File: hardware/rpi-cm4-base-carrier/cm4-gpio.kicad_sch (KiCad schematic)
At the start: 5 parts

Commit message: Finished schematic
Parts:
- removed F?: 0ZCG0150AF2C, footprints:0ZCG0150AF2C, symbol 2020-11-06_00-20-18:0ZCG0150AF2C
- added CR1: SMBJ5.0A-TR, footprints:SMBJ5.0A-TR, symbol 2020-11-06_22-01-36:SMBJ5.0A-TR
- added D1: LED Green, LED_SMD:LED_0603_1608Metric, symbol Device:LED
- added D2: LED Red, LED_SMD:LED_0603_1608Metric, symbol Device:LED
- added J1: DNP, Connector_PinHeader_2.54mm:PinHeader_1x10_P2.54mm_Vertical, symbol Connector_Generic:Conn_01x10
- added J3: SM04B-SRSS-TB(LF)(SN), SM04B-SRSS-TB_LF__SN_:JST_SM04B-SRSS-TB(LF)(SN), symbol SM04B-SRSS-TB_LF__SN_:SM04B-SRSS-TB(LF)(SN)
- added JP1: SolderJumper_2_Open, Jumper:SolderJumper-2_P1.3mm_Open_RoundedPad1.0x1.5mm, symbol Jumper:SolderJumper_2_Open
- added R2, R6: 1k, Resistor_SMD:R_0603_1608Metric_Pad0.98x0.95mm_HandSolder, symbol Device:R
- added R3, R5: DNP, Resistor_SMD:R_0603_1608Metric_Pad0.98x0.95mm_HandSolder, symbol Device:R
- added U1: 74LVC1G07SE-7, Package_TO_SOT_SMD:SOT-353_SC-70-5, symbol CM4IO:74LVC1G07_copy
- J2: renamed from J?; footprint GCT_USB4105-GF-A -> USB4105-GF-A:GCT_USB4105-GF-A
- gave numbers to parts that had none: 2
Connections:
- net +3.3V: now also Module1.78 (GPIO_VREF(1.8v/3.3v_Input)), D1.2 (A), D2.2 (A), J1.1 (Pin_1), J3.2, R3.1, R5.1, U1.5 (VCC)
- net +5V: now also J2.A4/B9 (VBUS), J2.B4/A9 (VBUS), CR1.1
- net GND: now also CR1.2, J1.2 (Pin_2), J3.1, J3.4, JP1.2 (B), R5.2, U1.3 (GND)
- net EEPROM_nWP: now reaches Module1.20 (EEPROM_nWP)
- net EEPROM_nWP: now also JP1.1 (A)
- net nLED_Activity: now reaches Module1.21 (PI_nLED_Activity)
- net nLED_Activity: now also R2.2
- net GPIO7: now reaches Module1.37 (GPIO7)
- net GPIO7: now also J1.9 (Pin_9)
- net GPIO11: now reaches Module1.38 (GPIO11)
- net GPIO11: now also J1.7 (Pin_7)
- net GPIO8: now reaches Module1.39 (GPIO8)
- net GPIO8: now also J1.8 (Pin_8)
- net GPIO9: now reaches Module1.40 (GPIO9)
- net GPIO9: now also J1.6 (Pin_6)
- net GPIO10: now reaches Module1.44 (GPIO10)
- net GPIO10: now also J1.5 (Pin_5)
- net GPIO15: now reaches Module1.51 (GPIO15)
- net GPIO15: now also J1.4 (Pin_4)
- net GPIO14: now reaches Module1.55 (GPIO14)
- net GPIO14: now also J1.3 (Pin_3)
- net GPIO2: now reaches Module1.58 (GPIO2)
- net GPIO2: now also J3.3, R3.2
- net nRPIBOOT: now reaches Module1.93 (nRPIBOOT)
- net nRPIBOOT: now also J1.10 (Pin_10)
- net nPWR_LED: now reaches Module1.95 (nPI_LED_PWR)
- net nPWR_LED: now also U1.2
- new net: D2.1 (K), R6.1
- new net: J3.S1 (SHIELD), J3.S2 (SHIELD)
- new net: R6.2, U1.4
- new net: D1.1 (K), R2.1
- no-connect marks 6 -> 7
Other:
- note added: "Activity LED"
- note added: "I2C1_SCL"
- note added: "I2C1_SDA"
- note added: "PWR LED"
- note added: "SPI0_CE0"
- note added: "SPI0_CE1"
- note added: "SPI0_CLK"
- note added: "SPI0_MISO"
- note added: "SPI0_MOSI"
- note added: "UART0_RXD"
- note added: "UART0_TXD"
- note added: "nBOOT"
- moved on the sheet: J2, R1, R4

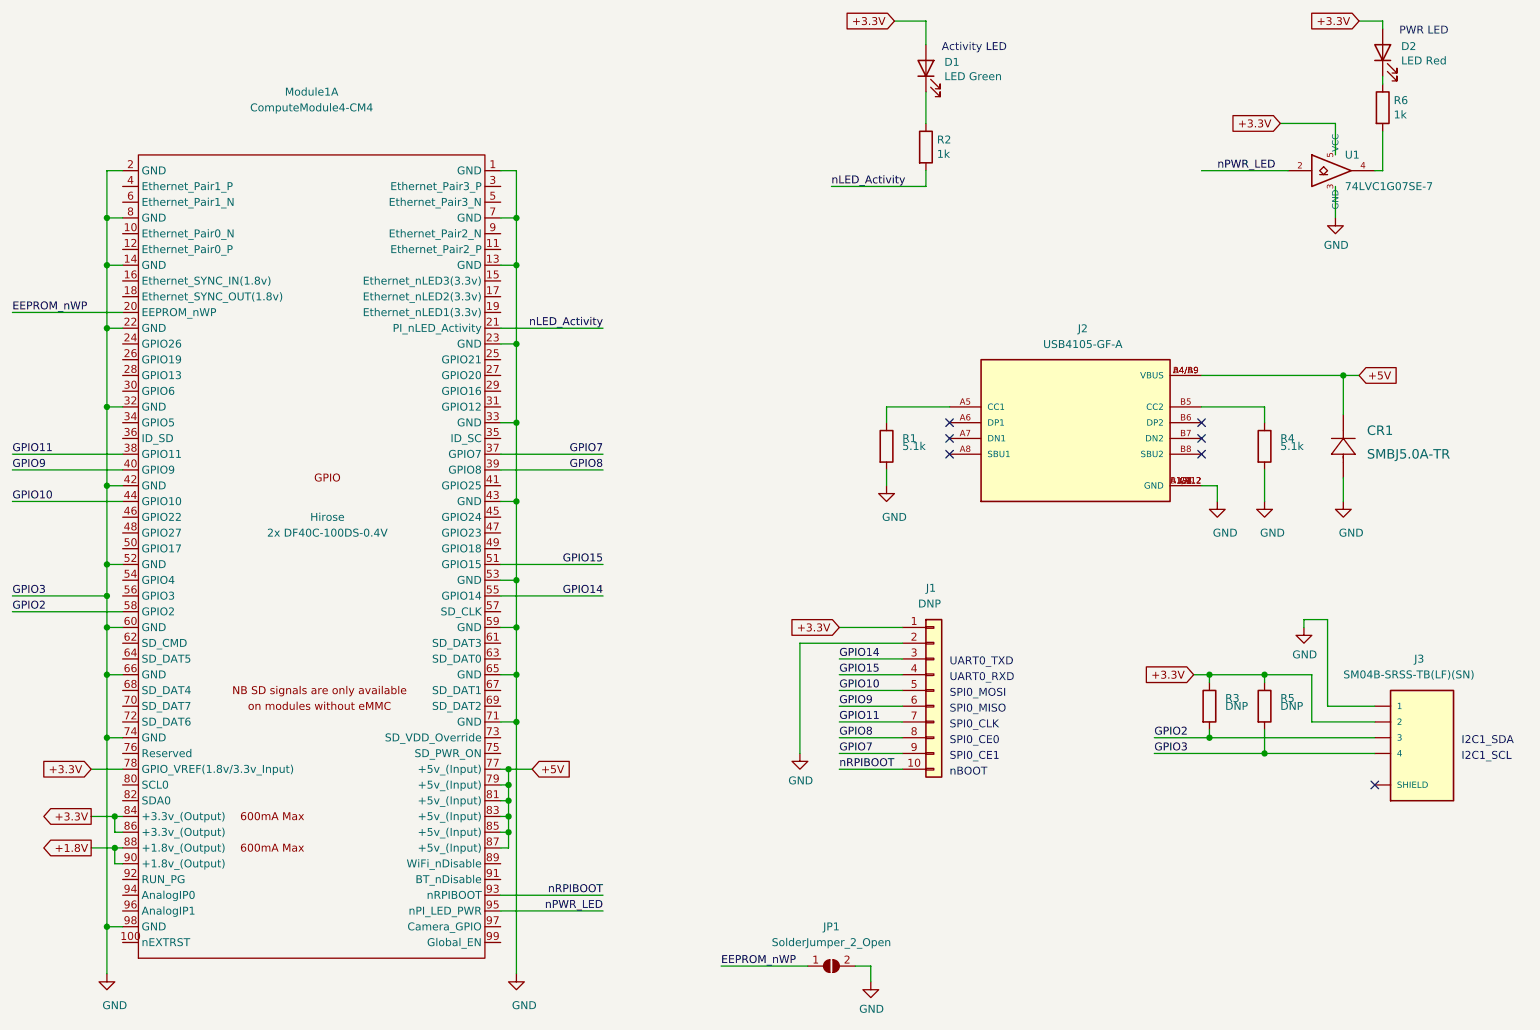
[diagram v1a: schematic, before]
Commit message: Added labels to schematic sections
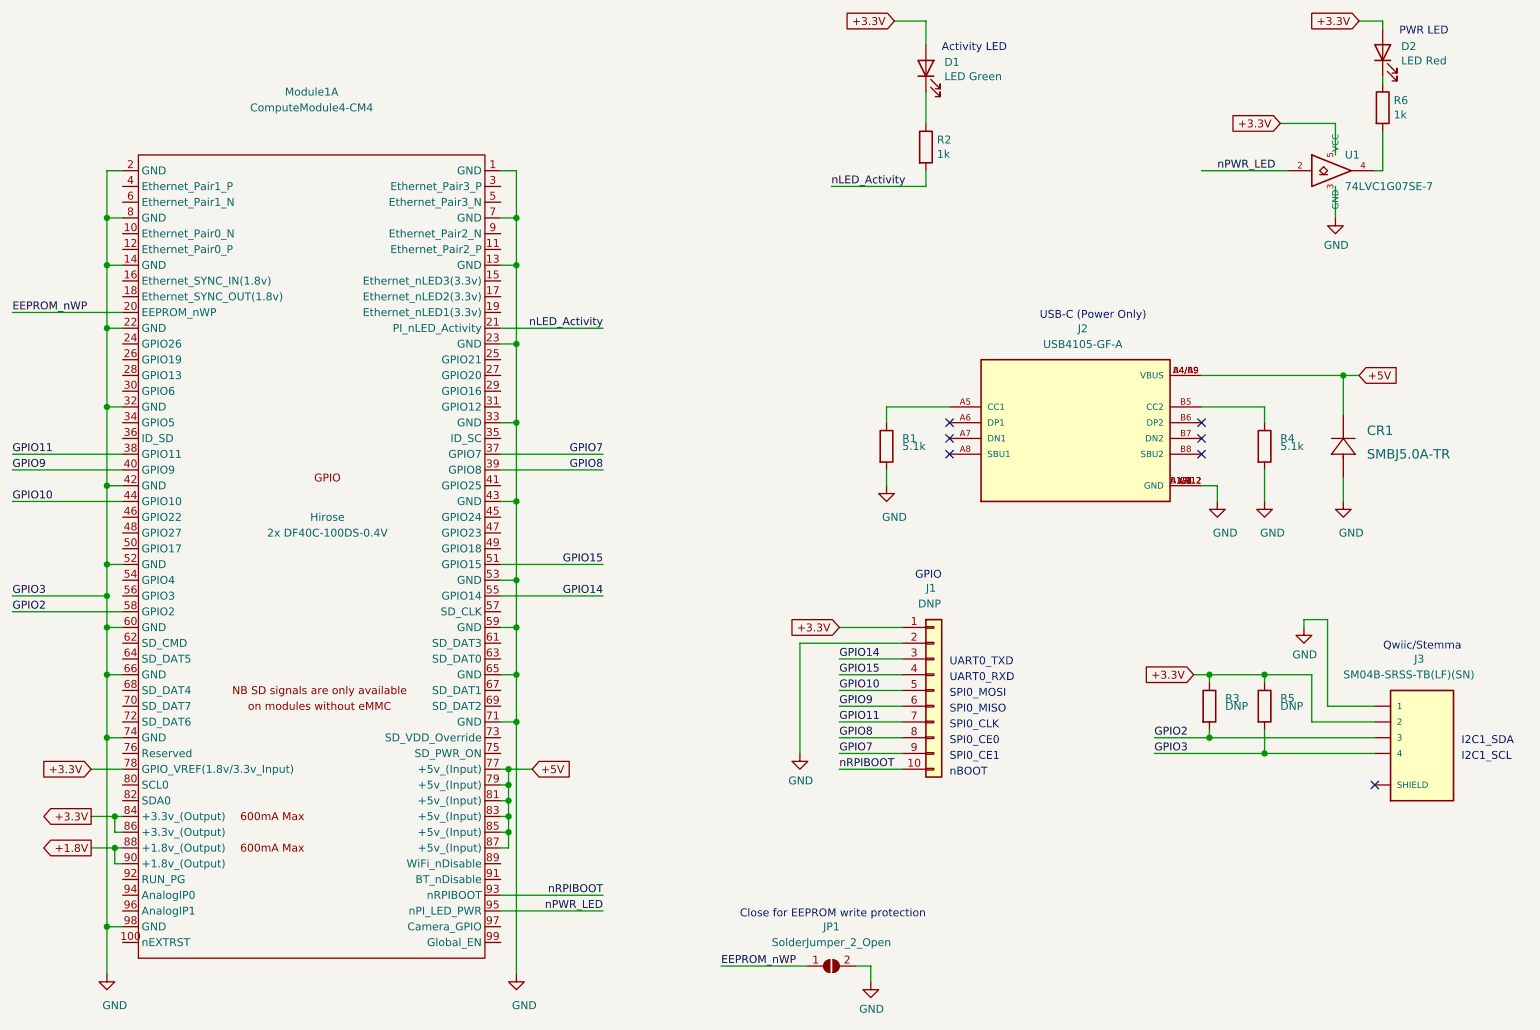
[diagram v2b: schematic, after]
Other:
- note added: "Close for EEPROM write protection"
- note added: "GPIO"
- note added: "Qwiic/Stemma"
- note added: "USB-C (Power Only)"
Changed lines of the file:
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@@
   (junction (at 227.33 139.7) (diameter 1.016) (color 0 0 0 0))
   (junction (at 240.03 78.74) (diameter 1.016) (color 0 0 0 0))
+  (no_connect (at 176.53 88.9))
+  (no_connect (at 217.17 88.9))
+  (no_connect (at 217.17 91.44))
   (no_connect (at 217.17 86.36))
-  (no_connect (at 217.17 88.9))
   (no_connect (at 245.11 144.78))
+  (no_connect (at 176.53 86.36))
   (no_connect (at 176.53 91.44))
-  (no_connect (at 176.53 86.36))
-  (no_connect (at 217.17 91.44))
-  (no_connect (at 176.53 88.9))
   (wire (pts (xy 25.4 68.58) (xy 43.18 68.58))
     (stroke (width 0) (type solid) (color 0 0 0 0))
@@
     (stroke (width 0) (type solid) (color 0 0 0 0))
   )
+  (text "Close for EEPROM write protection" (at 172.72 166.37 180)
+    (effects (font (size 1.27 1.27)) (justify right bottom))
+  )
   (text "Activity LED" (at 175.26 26.67 0)
     (effects (font (size 1.27 1.27)) (justify left bottom))
   )
+  (text "GPIO" (at 175.26 111.76 180)
+    (effects (font (size 1.27 1.27)) (justify right bottom))
+  )
   (text "UART0_TXD" (at 176.53 125.73 0)
     (effects (font (size 1.27 1.27)) (justify left bottom))
@@
     (effects (font (size 1.27 1.27)) (justify left bottom))
   )
+  (text "USB-C (Power Only)" (at 208.28 69.85 180)
+    (effects (font (size 1.27 1.27)) (justify right bottom))
+  )
   (text "PWR LED" (at 249.047 24.003 0)
     (effects (font (size 1.27 1.27)) (justify left bottom))
   )
+  (text "Qwiic/Stemma" (at 259.08 123.19 180)
+    (effects (font (size 1.27 1.27)) (justify right bottom))
+  )
   (text "I2C1_SDA" (at 259.08 138.43 0)

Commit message: Placed components
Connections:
- net GND: no longer J3.4, R5.2
- net GPIO3: now reaches Module1.56 (GPIO3)
- net GPIO3: now also J3.4, R5.2
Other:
- title: Raspberry Pi Compute Module 4 Carrier Template -> Raspberry Pi Compute Module 4 Base Carrier
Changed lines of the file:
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@@
   (paper "A4")
   (title_block
-    (title "Raspberry Pi Compute Module 4 Carrier Template")
+    (title "Raspberry Pi Compute Module 4 Base Carrier")
     (date "2020-10-31")
     (rev "v01")
@@
   (junction (at 40.64 96.52) (diameter 1.016) (color 0 0 0 0))
   (junction (at 40.64 109.22) (diameter 1.016) (color 0 0 0 0))
-  (junction (at 40.64 114.3) (diameter 1.016) (color 0 0 0 0))
   (junction (at 40.64 119.38) (diameter 1.016) (color 0 0 0 0))
   (junction (at 40.64 127) (diameter 1.016) (color 0 0 0 0))
@@
   (junction (at 240.03 78.74) (diameter 1.016) (color 0 0 0 0))
   (no_connect (at 176.53 88.9))
+  (no_connect (at 217.17 86.36))
+  (no_connect (at 217.17 91.44))
+  (no_connect (at 176.53 91.44))
+  (no_connect (at 245.11 144.78))
   (no_connect (at 217.17 88.9))
-  (no_connect (at 217.17 91.44))
-  (no_connect (at 217.17 86.36))
-  (no_connect (at 245.11 144.78))
   (no_connect (at 176.53 86.36))
-  (no_connect (at 176.53 91.44))
   (wire (pts (xy 25.4 68.58) (xy 43.18 68.58))
     (stroke (width 0) (type solid) (color 0 0 0 0))
@@
     (stroke (width 0) (type solid) (color 0 0 0 0))
   )
-  (wire (pts (xy 25.4 114.3) (xy 40.64 114.3))
+  (wire (pts (xy 25.4 114.3) (xy 43.18 114.3))
     (stroke (width 0) (type solid) (color 0 0 0 0))
   )
@@
     (stroke (width 0) (type solid) (color 0 0 0 0))
   )
-  (wire (pts (xy 40.64 109.22) (xy 40.64 114.3))
+  (wire (pts (xy 40.64 109.22) (xy 40.64 119.38))
     (stroke (width 0) (type solid) (color 0 0 0 0))
   )
@@
     (stroke (width 0) (type solid) (color 0 0 0 0))
   )
-  (wire (pts (xy 40.64 114.3) (xy 40.64 119.38))
-    (stroke (width 0) (type solid) (color 0 0 0 0))
-  )
